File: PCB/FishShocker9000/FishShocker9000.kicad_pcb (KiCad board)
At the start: 2 copper layers, 140 x 285.9 mm, 206 parts, among them J1 Barrel_Jack, J10 P70-1000045R, J100 P70-1000045R, J101 P70-1000045R, J102 P70-1000045R, J103 P70-1000045R, J104 P70-1000045R, J105 P70-1000045R, J106 P70-1000045R, J107 P70-1000045R, J108 P70-1000045R, J109 P70-1000045R, J11 P70-1000045R, J110 P70-1000045R, J111 P70-1000045R, J112 P70-1000045R, J113 P70-1000045R, J114 P70-1000045R, J115 P70-1000045R, J116 P70-1000045R, J117 P70-1000045R, J118 P70-1000045R, J119 P70-1000045R, J12 P70-1000045R, J120 P70-1000045R, J121 P70-1000045R, J122 P70-1000045R, J123 P70-1000045R, J124 P70-1000045R, J125 P70-1000045R, J126 P70-1000045R, J127 P70-1000045R, J128 P70-1000045R, J129 P70-1000045R, J13 P70-1000045R, J130 P70-1000045R, J131 P70-1000045R, J132 P70-1000045R, J133 P70-1000045R, J134 P70-1000045R, J135 P70-1000045R, J136 P70-1000045R, J137 P70-1000045R, J138 P70-1000045R, J139 P70-1000045R, J14 P70-1000045R, J140 P70-1000045R, J141 P70-1000045R, J142 P70-1000045R, J143 P70-1000045R, J144 P70-1000045R, J145 P70-1000045R, J146 Conn_01x03_Pin, J15 P70-1000045R, J16 P70-1000045R, J17 P70-1000045R, J18 P70-1000045R, J19 P70-1000045R, J2 P70-1000045R, J20 P70-1000045R, J21 P70-1000045R, J22 P70-1000045R, J23 P70-1000045R, J24 P70-1000045R, J25 P70-1000045R, J26 P70-1000045R, J27 P70-1000045R, J28 P70-1000045R, J29 P70-1000045R, J3 P70-1000045R, J30 P70-1000045R, J31 P70-1000045R, J32 P70-1000045R, J33 P70-1000045R, J34 P70-1000045R, J35 P70-1000045R, J36 P70-1000045R, J37 P70-1000045R, J38 P70-1000045R, J39 P70-1000045R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

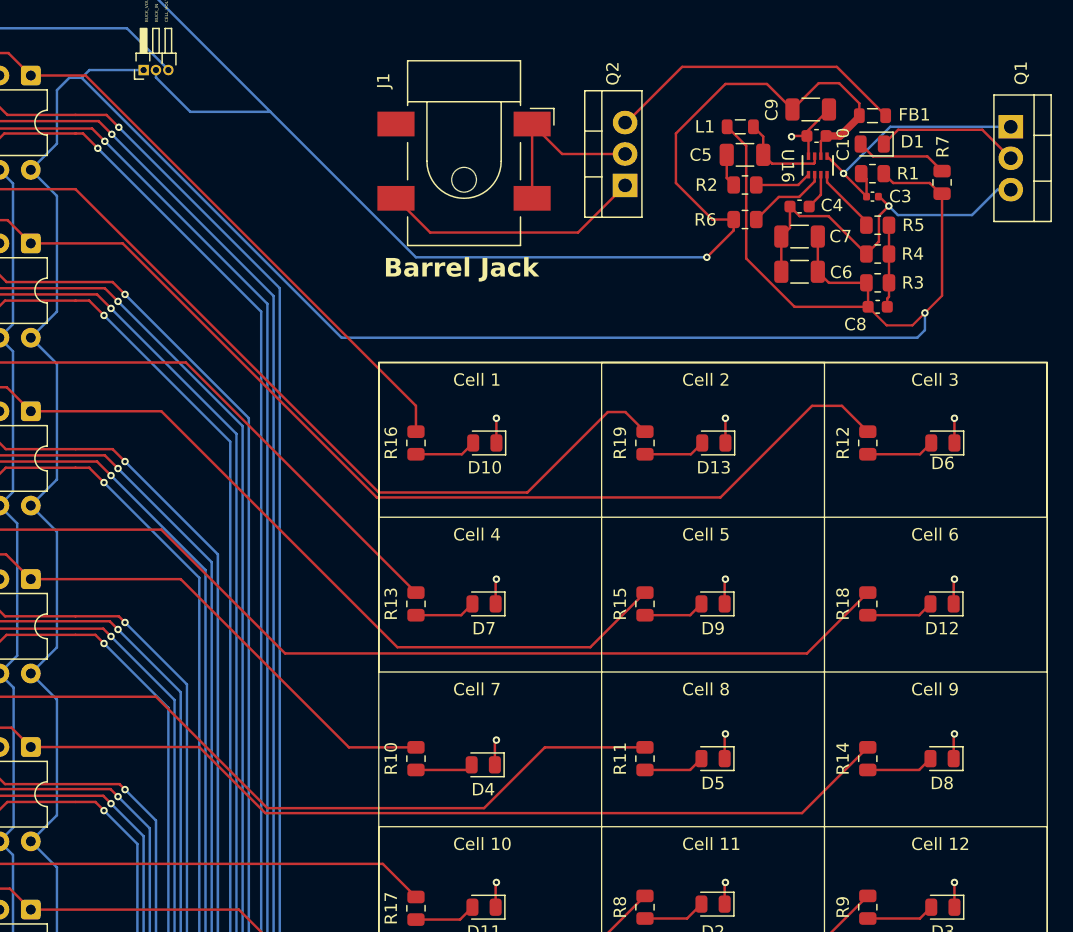
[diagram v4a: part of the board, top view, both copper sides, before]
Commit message: Fixed Corruption issues
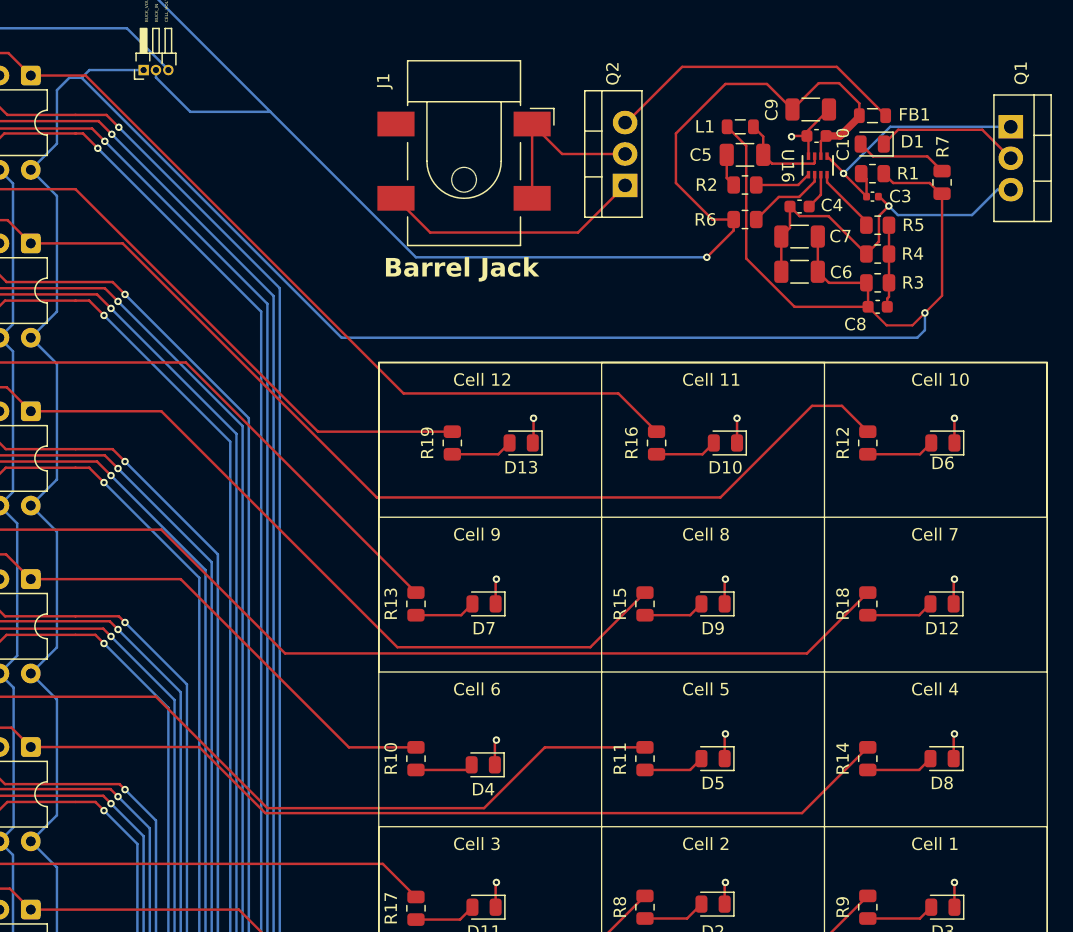
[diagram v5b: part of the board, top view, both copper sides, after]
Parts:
- moved D10 19.4 mm to (375.5, 117.0)
- moved R16 19.4 mm to (369.9, 117.0)
- moved D13 15.6 mm to (359.0, 117.0)
- moved R19 15.6 mm to (353.4, 117.0)
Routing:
- net CELL_12: track 135.5 -> 114.5 mm
- net CELL_11: track 121.1 -> 139.3 mm
- net GND: track 226.1 -> 225.6 mm
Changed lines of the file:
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@@
 	(footprint "Resistor_SMD:R_0805_2012Metric"
 		(layer "F.Cu")
-		(at 350.5 117 -90)
+		(at 369.9375 117 -90)
 		(descr "Resistor SMD 0805 (2012 Metric), square (rectangular) end terminal, IPC-7351 nominal, (Body size source: IPC-SM-782 page 72, https://www.pcb-3d.com/wordpress/wp-content/uploads/ipc-sm-782a_amendment_1_and_2.pdf), generated with kicad-footprint-generator")
 		(tags "resistor")
@@
 	(footprint "LED_SMD:LED_0805_2012Metric"
 		(layer "F.Cu")
-		(at 374.5625 117 180)
+		(at 359 117 180)
 		(descr "LED SMD 0805 (2012 Metric), square (rectangular) end terminal, IPC-7351 nominal, (Body size source: https://docs.google.com/spreadsheets/d/1BsfQQcO9C6DZCsRaXUlFlo91Tg2WpOkGARC1WS5S8t0/edit?usp=sharing), generated with kicad-footprint-generator")
 		(tags "LED")
@@
 	(footprint "LED_SMD:LED_0805_2012Metric"
 		(layer "F.Cu")
-		(at 356.0625 117 180)
+		(at 375.5 117 180)
 		(descr "LED SMD 0805 (2012 Metric), square (rectangular) end terminal, IPC-7351 nominal, (Body size source: https://docs.google.com/spreadsheets/d/1BsfQQcO9C6DZCsRaXUlFlo91Tg2WpOkGARC1WS5S8t0/edit?usp=sharing), generated with kicad-footprint-generator")
 		(tags "LED")
@@
 	(footprint "Resistor_SMD:R_0805_2012Metric"
 		(layer "F.Cu")
-		(at 369 117 -90)
+		(at 353.4375 117 -90)
 		(descr "Resistor SMD 0805 (2012 Metric), square (rectangular) end terminal, IPC-7351 nominal, (Body size source: IPC-SM-782 page 72, https://www.pcb-3d.com/wordpress/wp-content/uploads/ipc-sm-782a_amendment_1_and_2.pdf), generated with kicad-footprint-generator")
 		(tags "resistor")
@@
 		(layer "Edge.Cuts")
 	)
-	(gr_text "Cell 1"
+	(gr_text "Cell 12"
 		(at 353.5 112.5 0)
 		(layer "F.SilkS")
@@
 		)
 	)
-	(gr_text "Cell 3"
+	(gr_text "Cell 10"
 		(at 390.5 112.5 0)
 		(layer "F.SilkS")
@@
 		)
 	)
-	(gr_text "Cell 8"
+	(gr_text "Cell 5"
 		(at 372 137.5 0)
 		(layer "F.SilkS")
@@
 		)
 	)
-	(gr_text "Cell 10"
+	(gr_text "Cell 3"
 		(at 353.5 150 0)
 		(layer "F.SilkS")
@@
 		)
 	)
-	(gr_text "Cell 7"
+	(gr_text "Cell 6"
 		(at 353.5 137.5 0)
 		(layer "F.SilkS")
@@
 		)
 	)
-	(gr_text "Cell 6"
+	(gr_text "Cell 7"
 		(at 390.5 125 0)
 		(layer "F.SilkS")
@@
 		)
 	)
-	(gr_text "Cell 12"
+	(gr_text "Cell 1"
 		(at 390.5 150 0)
 		(layer "F.SilkS")
@@
 		)
 	)
-	(gr_text "Cell 5"
+	(gr_text "Cell 8"
 		(at 372 125 0)
 		(layer "F.SilkS")
@@
 		)
 	)
-	(gr_text "Cell 4"
+	(gr_text "Cell 9"
 		(at 353.5 125 0)
 		(layer "F.SilkS")
@@
 		)
 	)
-	(gr_text "Cell 9"
+	(gr_text "Cell 4"
 		(at 390.5 137.5 0)
 		(layer "F.SilkS")
@@
 		)
 	)
-	(gr_text "Cell 11"
+	(gr_text "Cell 2"
 		(at 372 150 0)
 		(layer "F.SilkS")
@@
 		)
 	)
-	(gr_text "Cell 2"
+	(gr_text "Cell 11"
 		(at 372 112.5 0)
 		(layer "F.SilkS")
@@
 	)
 	(segment
-		(start 350.5 117.9125)
-		(end 354.2125 117.9125)
+		(start 369.9375 117.9125)
+		(end 373.65 117.9125)
 		(width 0.2)
 		(layer "F.Cu")
@@
 	)
 	(segment
-		(start 354.2125 117.9125)
-		(end 355.125 117)
+		(start 373.65 117.9125)
+		(end 374.5625 117)
 		(width 0.2)
 		(layer "F.Cu")
@@
 	)
 	(segment
-		(start 369 117.9125)
-		(end 372.7125 117.9125)
+		(start 353.4375 117.9125)
+		(end 357.15 117.9125)
 		(width 0.2)
 		(layer "F.Cu")
@@
 	)
 	(segment
-		(start 372.7125 117.9125)
-		(end 373.625 117)
+		(start 357.15 117.9125)
+		(end 358.0625 117)
 		(width 0.2)
 		(layer "F.Cu")
@@
 	)
 	(segment
-		(start 319.39 87.317)
-		(end 323.817 87.317)
+		(start 366.85 113)
+		(end 369.9375 116.0875)
+		(width 0.2)
+		(layer "F.Cu")
+		(net 42)
+	)
+	(segment
+		(start 323.817 87.317)
+		(end 349.5 113)
 		(width 0.2)
 		(layer "F.Cu")
@@
 	)
 	(segment
-		(start 323.817 87.317)
-		(end 350.5 114)
+		(start 349.5 113)
+		(end 366.85 113)
 		(width 0.2)
 		(layer "F.Cu")
@@
 	)
 	(segment
-		(start 350.5 114)
-		(end 350.5 116.0875)
+		(start 319.39 87.317)
+		(end 323.817 87.317)
 		(width 0.2)
 		(layer "F.Cu")
@@
 	)
 	(segment
-		(start 301.61 94.937)
-		(end 303.173 96.5)
+		(start 301.047 95.5)
+		(end 301.61 94.937)
 		(width 0.2)
 		(layer "F.Cu")
@@
 	)
 	(segment
-		(start 301.047 95.5)
-		(end 301.61 94.937)
+		(start 342.5875 116.0875)
+		(end 353.4375 116.0875)
 		(width 0.2)
 		(layer "F.Cu")
@@
 	)
 	(segment
-		(start 359.5 121)
-		(end 366 114.5)
+		(start 323 96.5)
+		(end 342.5875 116.0875)
 		(width 0.2)
 		(layer "F.Cu")
@@
 	)
 	(segment
-		(start 347.5 121)
-		(end 359.5 121)
-		(width 0.2)
-		(layer "F.Cu")
-		(net 45)
-	)
-	(segment
-		(start 366 114.5)
-		(end 367.4125 114.5)
-		(width 0.2)
-		(layer "F.Cu")
-		(net 45)
-	)
-	(segment
-		(start 367.4125 114.5)
-		(end 369 116.0875)
-		(width 0.2)
-		(layer "F.Cu")
-		(net 45)
-	)
-	(segment
-		(start 323 96.5)
-		(end 347.5 121)
+		(start 301.61 94.937)
+		(end 303.173 96.5)
 		(width 0.2)
 		(layer "F.Cu")
@@
 	)
 	(segment
+		(start 360 116.5)
+		(end 360 115)
+		(width 0.2)
+		(layer "F.Cu")
+		(net 110)
+	)
+	(segment
 		(start 375.4375 152.5625)
 		(end 375.5 152.5)
@@
 	)
 	(segment
-		(start 357 117)
-		(end 357 115)
+		(start 376.4375 117)
+		(end 376.4375 115)
 		(width 0.2)
 		(layer "F.Cu")
@@
 	)
 	(segment
-		(start 375.5 117)
-		(end 375.5 115)
-		(width 0.2)
-		(layer "F.Cu")
-		(net 110)
-	)
-	(segment
 		(start 309.23 114.439)
 		(end 309.23 122.059)
@@
 	)
 	(via
-		(at 375.5 115)
-		(size 0.6)
-		(drill 0.3)
-		(layers "F.Cu" "B.Cu")
-		(net 110)
-	)
-	(via
-		(at 357 115)
+		(at 376.4375 115)
 		(size 0.6)
 		(drill 0.3)
@@
 		(size 0.6)
 		(drill 0.3)
+		(layers "F.Cu" "B.Cu")
+		(net 110)
+	)
+	(via
+		(at 360 115)
+		(size 0.6)
+		(drill 0.3)
